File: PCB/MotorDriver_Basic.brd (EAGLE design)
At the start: 47.5 x 26.4 mm, 20 parts, among them J2 MTR_CTRL, J3 MCU PWR, J4 MTR PWR

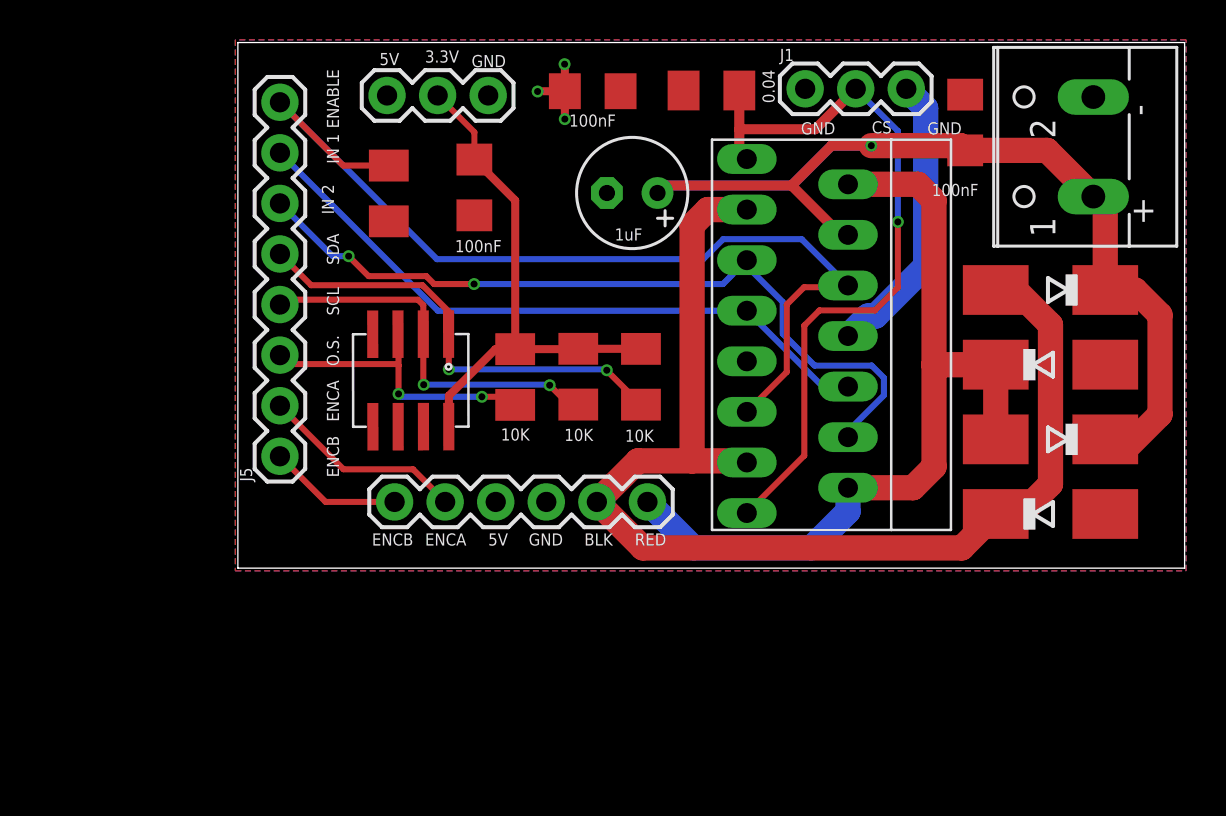
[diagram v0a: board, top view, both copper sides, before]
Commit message: added the motor driver to schematic.
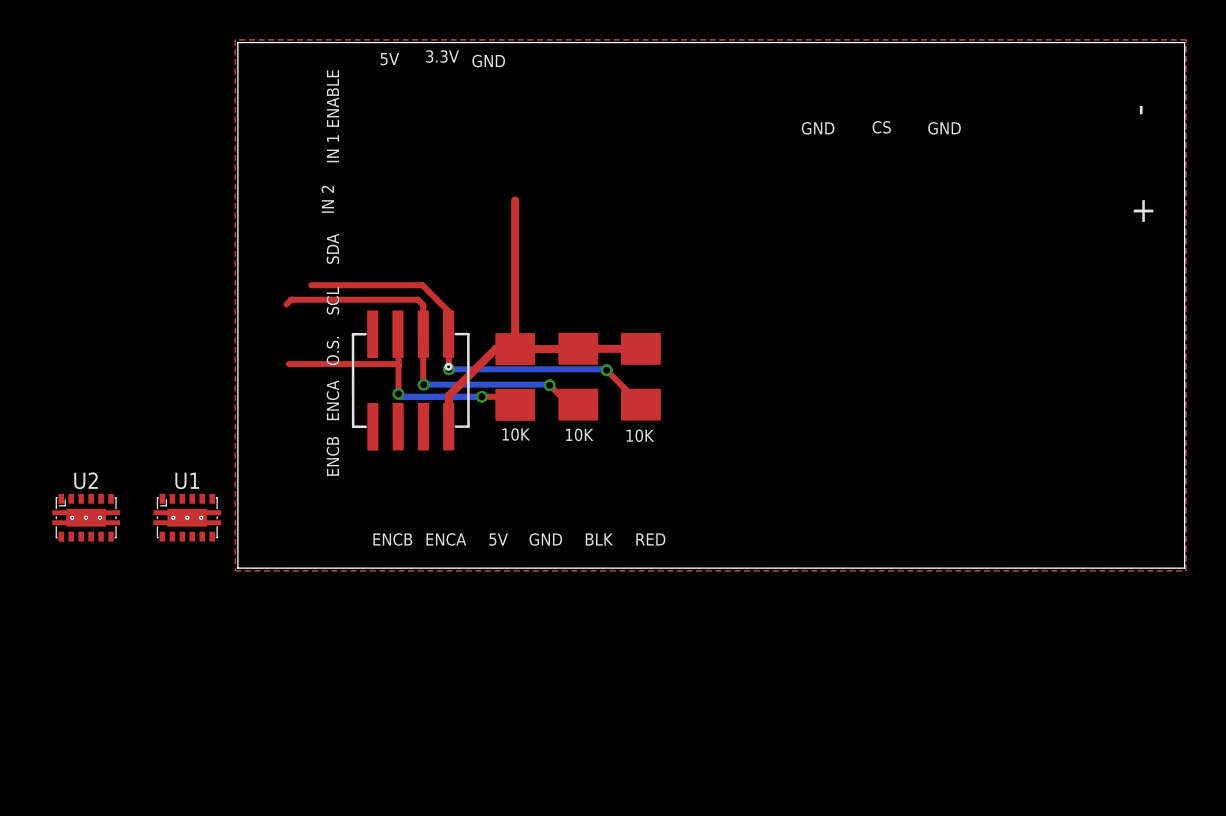
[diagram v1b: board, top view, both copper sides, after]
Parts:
- removed C1: 1uF, rcl:E2,5-6
- removed C2, C3, C4: 100nF, rcl:C1206
- removed J1: (no value), SparkFun-Connectors:1X03
- removed J2: MTR_CTRL, SparkFun-Connectors:1X06
- removed J3: MCU PWR, SparkFun-Connectors:1X03
- removed J4: MTR PWR, L298_Motor_Driver_Lib_ECE5780:W237-102
- removed J5: (no value), SparkFun-Connectors:1X08
- removed R1: 10K, rcl:M1206
- removed R2: 0.04, rcl:M1206
- removed U$1: L298N-MULTIWATT15, ECE5780-MotorDriver:L298N-MULTIWATT15
- removed U$5, U$6, U$7, U$8: SS14CT-ND, L298_Motor_Driver_Lib_ECE5780:SOD106A-W
- added U1, U2: DRV8835, bt_motordriver:WSON_2X3
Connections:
- removed net 5V: C4.1, J2.3, J3.3, U$1.9
- removed net CS: J1.2, R2.1, U$1.1, U$1.15
- removed net ENABLE: J5.8, R1.2, U$1.11, U$1.6
- removed net ENC_A: J2.2, J5.2
- removed net ENC_B: J2.1, J5.1
- removed net IN_1: J5.7, U$1.10, U$1.7
- removed net IN_2: J5.6, U$1.12, U$1.5
- removed net MTR_BLK: J2.5, U$1.13, U$1.3, U$5.A, U$6.C
- removed net MTR_RED: J2.6, U$1.14, U$1.2, U$7.A, U$8.C
- removed net VCC: C1.+, C2.1, J4.1, U$1.4, U$5.C, U$7.C
- net 3.3V: no longer C3.1, J3.2
- net GND: no longer C1.-, C2.2, C3.2, C4.2, J1.1, J1.3, J2.4, J3.1, J4.2, R1.1, R2.2, U$1.8, U$6.A, U$8.A
- net O.S.: no longer J5.3
- net SCL: no longer J5.4
- net SDA: no longer J5.5
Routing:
- net MTR_BLK: track 61.3 -> 0.00 mm
- net VCC: track 57.6 -> 0.00 mm, vias 1 -> 0
- net ENABLE: track 49.7 -> 0.00 mm
- net MTR_RED: track 43.0 -> 0.00 mm
- net IN_2: track 39.8 -> 0.00 mm, vias 2 -> 0
- net CS: track 37.2 -> 0.00 mm, vias 1 -> 0
- net IN_1: track 33.4 -> 0.00 mm
- net GND: track 14.7 -> 0.00 mm
- net ENC_A: track 10.3 -> 0.00 mm
- net 3.3V: track 26.5 -> 19.6 mm
- net ENC_B: track 6.71 -> 0.00 mm
- net 5V: track 4.14 -> 0.00 mm, vias 3 -> 0
- net SDA: track 23.0 -> 20.8 mm
- net O.S.: track 15.3 -> 14.6 mm

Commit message: Finished the Schematic.
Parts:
- removed U2: DRV8835, bt_motordriver:WSON_2X3
- added C1, C3: 0.1 uF, rcl:C1206
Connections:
- new net IN1: U1.10, U1.8
- new net IN2: U1.7, U1.9
- new net MOUTA1: U1.2
- new net MOUTA2: U1.3
- new net MOUTB1: U1.4
- new net MOUTB2: U1.5
- new net VCC: C3.1, U1.11
- new net VM: C1.1, U1.1
- net GND: now also C1.2, C3.2, U1.6, U1.PAD, U1.PAD1, U1.PAD2, U1.PAD3, U1.PAD4
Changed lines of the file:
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@@
 <attribute name="VALUE" x="33.147" y="26.363" size="0.8128" layer="27" font="vector" rot="R180" align="bottom-center"/>
 </element>
-<element name="U2" library="bt_motordriver" package="WSON_2X3" value="DRV8835" x="28.067" y="27.813" smashed="yes">
-<attribute name="NAME" x="28.067" y="29.263" size="0.8128" layer="25" font="vector" align="bottom-center"/>
-<attribute name="VALUE" x="28.067" y="26.363" size="0.8128" layer="27" font="vector" rot="R180" align="bottom-center"/>
+<element name="C3" library="rcl" library_urn="urn:adsk.eagle:library:334" package="C1206" package3d_urn="urn:adsk.eagle:package:23618/2" value="0.1 uF" x="27.94" y="21.971" smashed="yes">
+<attribute name="NAME" x="26.67" y="23.241" size="1.27" layer="25"/>
+<attribute name="SPICEPREFIX" value="C" x="27.94" y="21.971" size="1.778" layer="27" display="off"/>
+<attribute name="VALUE" x="26.67" y="19.431" size="1.27" layer="27"/>
+</element>
+<element name="C1" library="rcl" library_urn="urn:adsk.eagle:library:334" package="C1206" package3d_urn="urn:adsk.eagle:package:23618/2" value="0.1 uF" x="27.94" y="15.748" smashed="yes">
+<attribute name="NAME" x="26.67" y="17.018" size="1.27" layer="25"/>
+<attribute name="SPICEPREFIX" value="C" x="27.94" y="15.748" size="1.778" layer="27" display="off"/>
+<attribute name="VALUE" x="26.67" y="13.208" size="1.27" layer="27"/>
 </element>
 </elements>
@@
 <vertex x="35.56" y="51.816"/>
 </polygon>
+<contactref element="C3" pad="2"/>
+<contactref element="C1" pad="2"/>
+<contactref element="U1" pad="PAD4"/>
+<contactref element="U1" pad="PAD3"/>
+<contactref element="U1" pad="PAD2"/>
+<contactref element="U1" pad="PAD1"/>
+<contactref element="U1" pad="PAD"/>
+<contactref element="U1" pad="6"/>
 <wire x1="42.4683875" y1="32.3816" x2="42.460275" y2="37.029590625" width="0" layer="19" extent="1-1"/>
 <wire x1="43.738384375" y1="32.383815625" x2="42.4683875" y2="32.3816" width="0" layer="19" extent="1-1"/>
 <wire x1="45.008384375" y1="32.38603125" x2="43.738384375" y2="32.383815625" width="0" layer="19" extent="1-1"/>
+<wire x1="34.497" y1="28.063" x2="42.4683875" y2="32.3816" width="0" layer="19" extent="1-1"/>
+<wire x1="34.497" y1="27.563" x2="34.497" y2="28.063" width="0" layer="19" extent="1-1"/>
+<wire x1="34.397" y1="26.863" x2="34.497" y2="27.563" width="0" layer="19" extent="1-1"/>
+<wire x1="33.147" y1="27.813" x2="34.497" y2="28.063" width="0" layer="19" extent="1-1"/>
+<wire x1="31.797" y1="28.063" x2="33.147" y2="27.813" width="0" layer="19" extent="1-1"/>
+<wire x1="31.797" y1="27.563" x2="31.797" y2="28.063" width="0" layer="19" extent="1-1"/>
+<wire x1="29.34" y1="21.971" x2="31.797" y2="27.563" width="0" layer="19" extent="1-1"/>
+<wire x1="29.34" y1="15.748" x2="29.34" y2="21.971" width="0" layer="19" extent="1-1"/>
 </signal>
 <signal name="5V">
@@
 <wire x1="49.615546875" y1="36.280475" x2="48.626171875" y2="36.280475" width="0.4064" layer="1"/>
 </signal>
+<signal name="VCC">
+<contactref element="U1" pad="11"/>
+<contactref element="C3" pad="1"/>
+<wire x1="26.54" y1="21.971" x2="32.397" y2="28.763" width="0" layer="19" extent="1-1"/>
+</signal>
+<signal name="VM">
+<contactref element="C1" pad="1"/>
+<contactref element="U1" pad="1"/>
+<wire x1="26.54" y1="15.748" x2="31.897" y2="26.863" width="0" layer="19" extent="1-1"/>
+</signal>
+<signal name="IN1">
+<contactref element="U1" pad="10"/>
+<contactref element="U1" pad="8"/>
+<wire x1="32.897" y1="28.763" x2="33.897" y2="28.763" width="0" layer="19" extent="1-1"/>
+</signal>
+<signal name="IN2">
+<contactref element="U1" pad="9"/>
+<contactref element="U1" pad="7"/>
+<wire x1="34.397" y1="28.763" x2="33.397" y2="28.763" width="0" layer="19" extent="1-1"/>
+</signal>
+<signal name="MOUTA1">
+<contactref element="U1" pad="2"/>
+</signal>
+<signal name="MOUTA2">
+<contactref element="U1" pad="3"/>
+</signal>
+<signal name="MOUTB1">
+<contactref element="U1" pad="4"/>
+</signal>
+<signal name="MOUTB2">
+<contactref element="U1" pad="5"/>
+</signal>
 </signals>
